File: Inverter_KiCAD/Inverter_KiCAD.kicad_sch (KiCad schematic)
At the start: 0 parts

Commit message: add break
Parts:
- added H1, H2, H3, H4, H5, H6, H7, H8: MountingHole_Pad, symbol Mechanical:MountingHole_Pad
- added J6: Conn_01x03, symbol Connector_Generic:Conn_01x03
- added J7: Conn_01x04, symbol Connector_Generic:Conn_01x04
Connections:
- net GND: now also H5.1, H6.1, H7.1, H8.1, J6.1 (Pin_1)
- net ISO_GND: now also H1.1, H2.1, H3.1, H4.1
- net U_output: now also J7.2 (Pin_2)
- net V_output: now also J7.3 (Pin_3)
- net W_output: now also J7.4 (Pin_4)
- new net Earth: J6.3 (Pin_3), J7.1 (Pin_1)
- new net VSupply_BB: J6.2 (Pin_2)
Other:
- added sheet break (break.kicad_sch)
- added sheet pwrSupplyFiltering (pwrSupplyFiltering.kicad_sch)
- sheet MCU_STM32G474 ports: added Bus_Imes, Bus_V, IC_PWN_U_H, IC_PWN_U_L, IC_PWN_V_H, IC_PWN_V_L, IC_PWN_W_H, IC_PWN_W_L, ISO_3V3, ISO_GND, ISO_PWM_Break, Nucleo_NRST, Nucleo_Rx, Nucleo_Tx, Pwr_Enable, U_Imes, U_VPh, V_Imes, V_VPh, W_Imes, W_VPh; removed none
- sheet Vbus_Sense ports: added ISO_3.3V, Imes, V_Bus_In, V_Bus_Out; removed VBus
- note added: "Break for reverse current protection"
- note added: "Bus mesurement Current and voltage"
- note added: "Chopper 3x Half-bridges"
- note added: "Input Supply and DC/DC converters"
- note added: "Isolated Side"
- note added: "Mounting Holes"
- note added: "NUCLEO for student programming"
- note added: "Power Side"
- note added: "STM32G474RET6 uC for signals analyse and protection Buttons, leds, screen and rotary encoder connectors"

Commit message: update
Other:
- note added: "Ventilateur Radiateur Mesure de température ???"
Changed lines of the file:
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@@
+    (effects (font (size 1.27 1.27)) (justify left bottom))
+  )
+  (text "Ventilateur\nRadiateur\nMesure de température ???" (at 13.97 171.45 0)
     (effects (font (size 1.27 1.27)) (justify left bottom))
   )

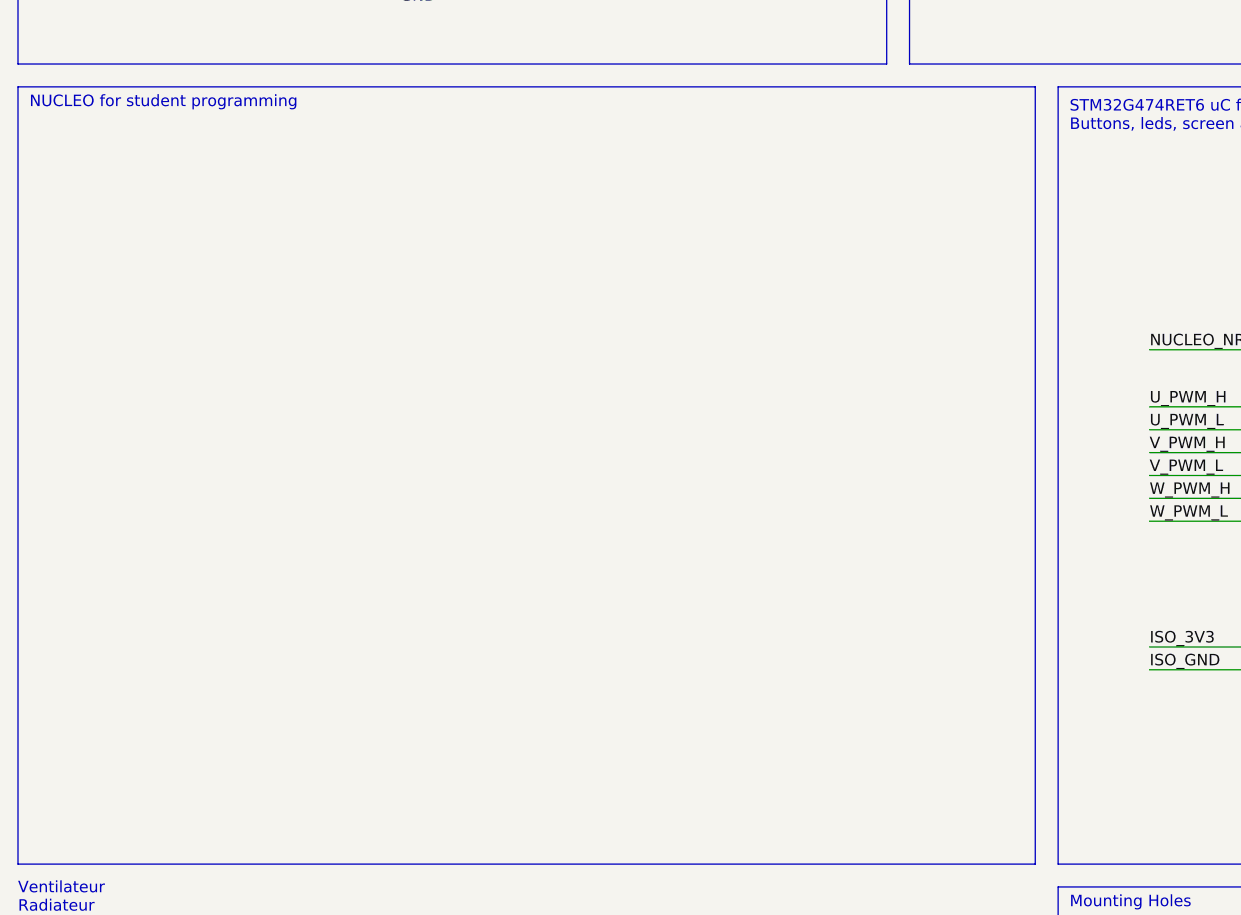
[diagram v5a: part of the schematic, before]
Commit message: start schematic Nucleo board
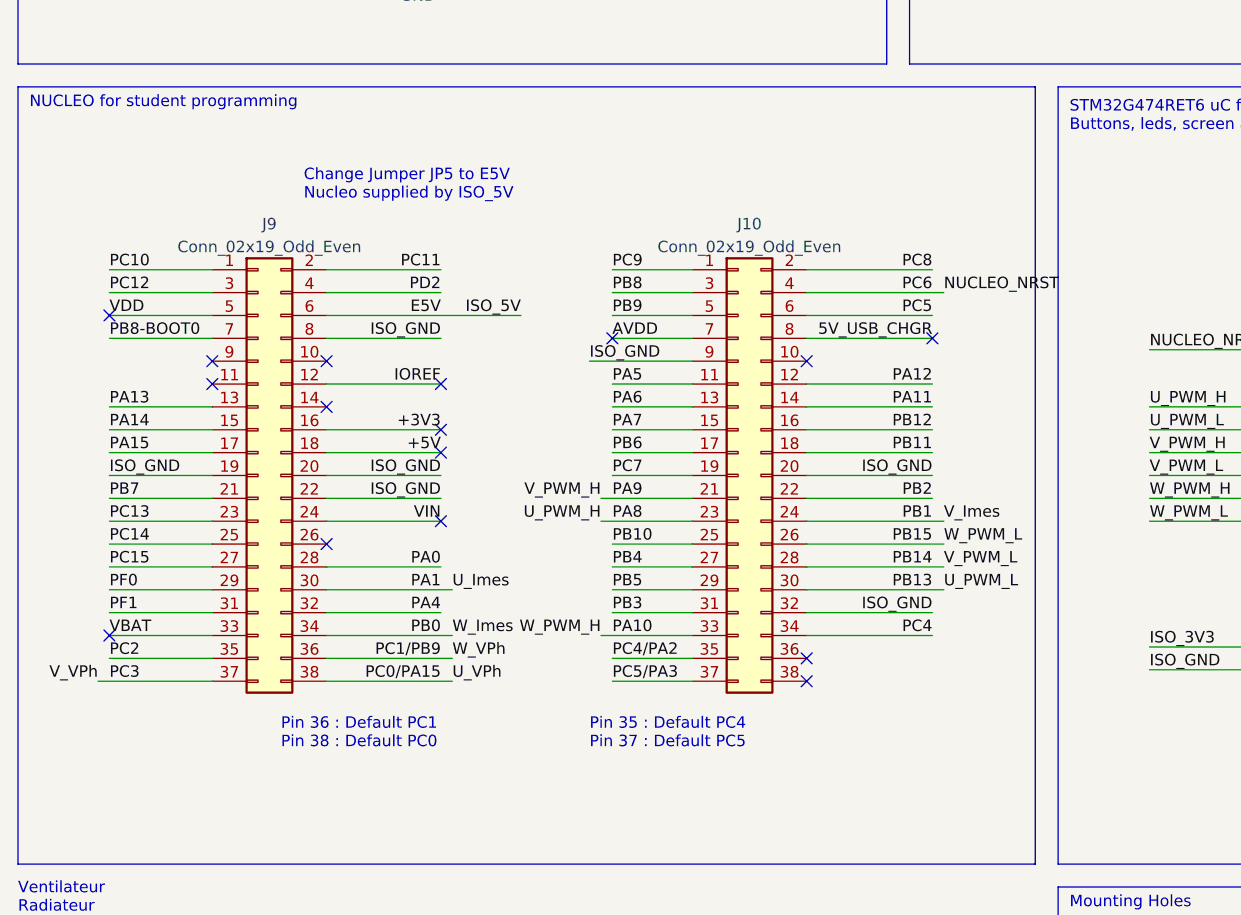
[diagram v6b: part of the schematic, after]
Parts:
- added J10, J9: Conn_02x19_Odd_Even, symbol Connector_Generic:Conn_02x19_Odd_Even
- H1, H2, H3, H4, H5, H6, H7, H8: footprint (none) -> MountingHole:MountingHole_3.2mm_M3_Pad_Via
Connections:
- net ISO_GND: now also J10.20 (Pin_20), J10.32 (Pin_32), J10.9 (Pin_9), J9.19 (Pin_19), J9.20 (Pin_20), J9.22 (Pin_22), J9.8 (Pin_8)
- net NUCLEO_NRST: now also J10.4 (Pin_4)
- new net +3V3: J9.16 (Pin_16)
- new net +5V: J9.18 (Pin_18)
- new net 5V_USB_CHGR: J10.8 (Pin_8)
- new net AVDD: J10.7 (Pin_7)
- new net E5V: J9.6 (Pin_6)
- new net IOREF: J9.12 (Pin_12)
- new net PA0: J9.28 (Pin_28)
- new net PA1: J9.30 (Pin_30)
- new net PA10: J10.33 (Pin_33)
- new net PA11: J10.14 (Pin_14)
- new net PA12: J10.12 (Pin_12)
- new net PA13: J9.13 (Pin_13)
- new net PA14: J9.15 (Pin_15)
- new net PA15: J9.17 (Pin_17)
- new net PA4: J9.32 (Pin_32)
- new net PA5: J10.11 (Pin_11)
- new net PA6: J10.13 (Pin_13)
- new net PA7: J10.15 (Pin_15)
- new net PA8: J10.23 (Pin_23)
- new net PA9: J10.21 (Pin_21)
- new net PB0: J9.34 (Pin_34)
- new net PB1: J10.24 (Pin_24)
- new net PB10: J10.25 (Pin_25)
- new net PB11: J10.18 (Pin_18)
- new net PB12: J10.16 (Pin_16)
- new net PB13: J10.30 (Pin_30)
- new net PB14: J10.28 (Pin_28)
- new net PB15: J10.26 (Pin_26)
- new net PB2: J10.22 (Pin_22)
- new net PB3: J10.31 (Pin_31)
- new net PB4: J10.27 (Pin_27)
- new net PB5: J10.29 (Pin_29)
- new net PB6: J10.17 (Pin_17)
- new net PB7: J9.21 (Pin_21)
- new net PB8: J10.3 (Pin_3)
- new net PB8-BOOT0: J9.7 (Pin_7)
- new net PB9: J10.5 (Pin_5)
- new net PC0/PA15: J9.38 (Pin_38)
- new net PC10: J9.1 (Pin_1)
- new net PC11: J9.2 (Pin_2)
- new net PC12: J9.3 (Pin_3)
- new net PC13: J9.23 (Pin_23)
- new net PC14: J9.25 (Pin_25)
- new net PC15: J9.27 (Pin_27)
- new net PC1/PB9: J9.36 (Pin_36)
- new net PC2: J9.35 (Pin_35)
- new net PC3: J9.37 (Pin_37)
- new net PC4: J10.34 (Pin_34)
- new net PC4/PA2: J10.35 (Pin_35)
- new net PC5: J10.6 (Pin_6)
- new net PC5/PA3: J10.37 (Pin_37)
- new net PC7: J10.19 (Pin_19)
- new net PC8: J10.2 (Pin_2)
- new net PC9: J10.1 (Pin_1)
- new net PD2: J9.4 (Pin_4)
- new net PF0: J9.29 (Pin_29)
- new net PF1: J9.31 (Pin_31)
- new net VBAT: J9.33 (Pin_33)
- new net VDD: J9.5 (Pin_5)
- new net VIN: J9.24 (Pin_24)
- no-connect marks 0 -> 16
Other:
- note added: "Change Jumper JP5 to E5V Nucleo supplied by ISO_5V"
- note added: "Pin 35 : Default PC4 Pin 37 : Default PC5"
- note added: "Pin 36 : Default PC1 Pin 38 : Default PC0"

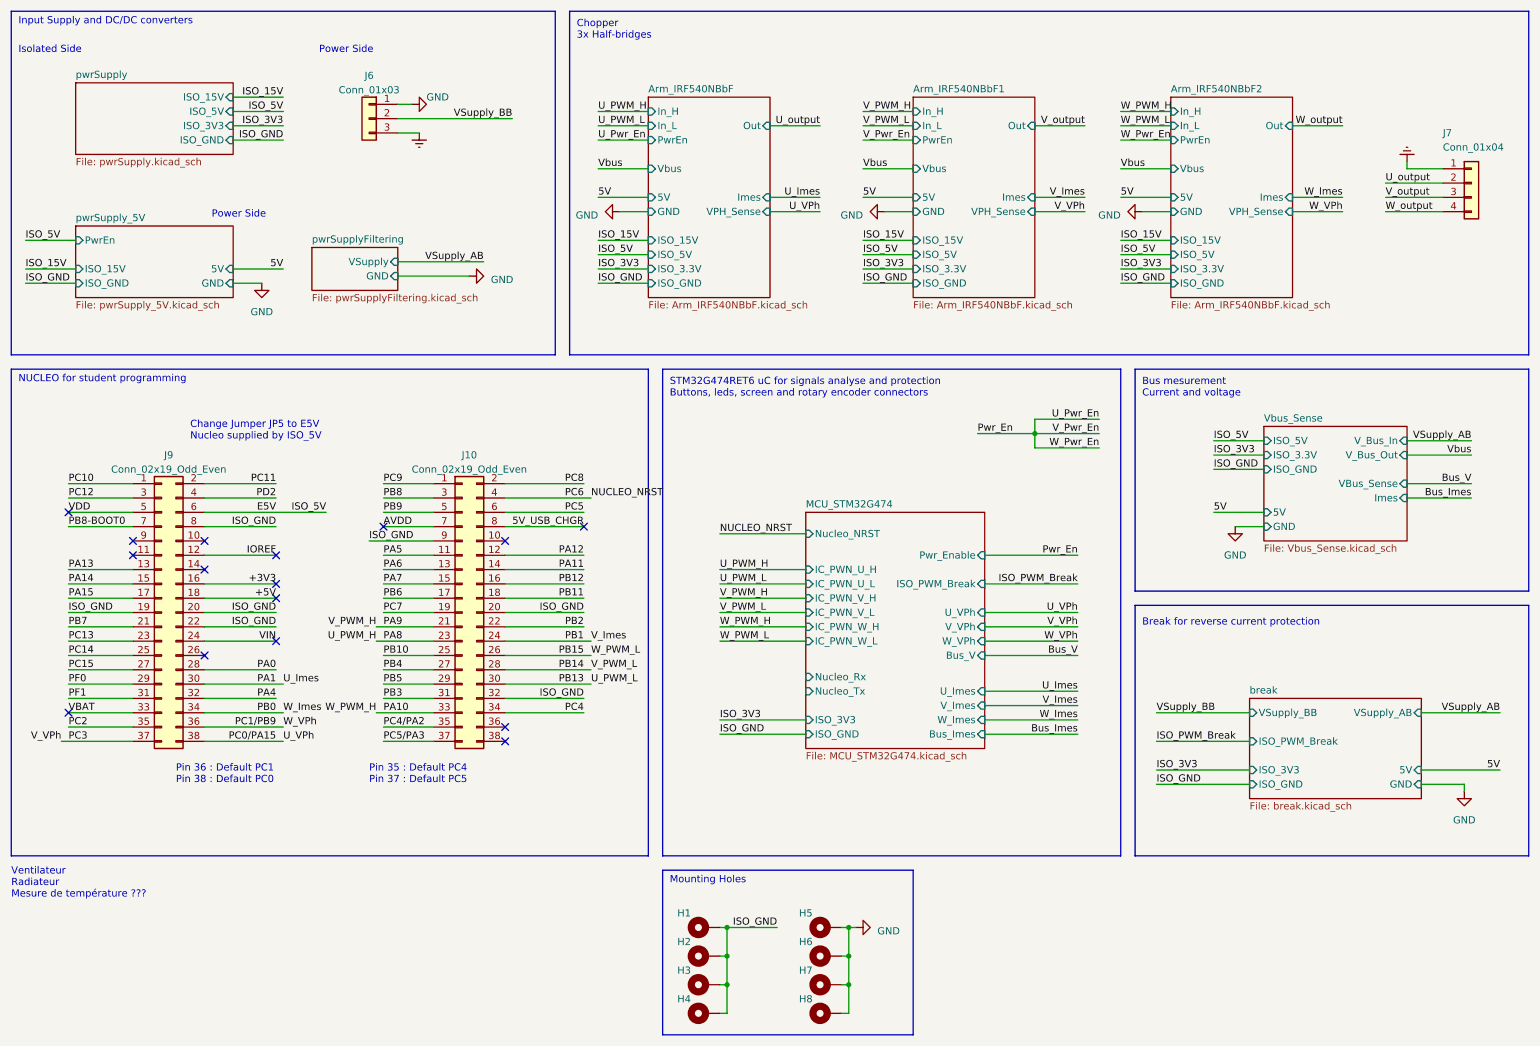
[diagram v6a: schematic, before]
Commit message: clear schematic errors
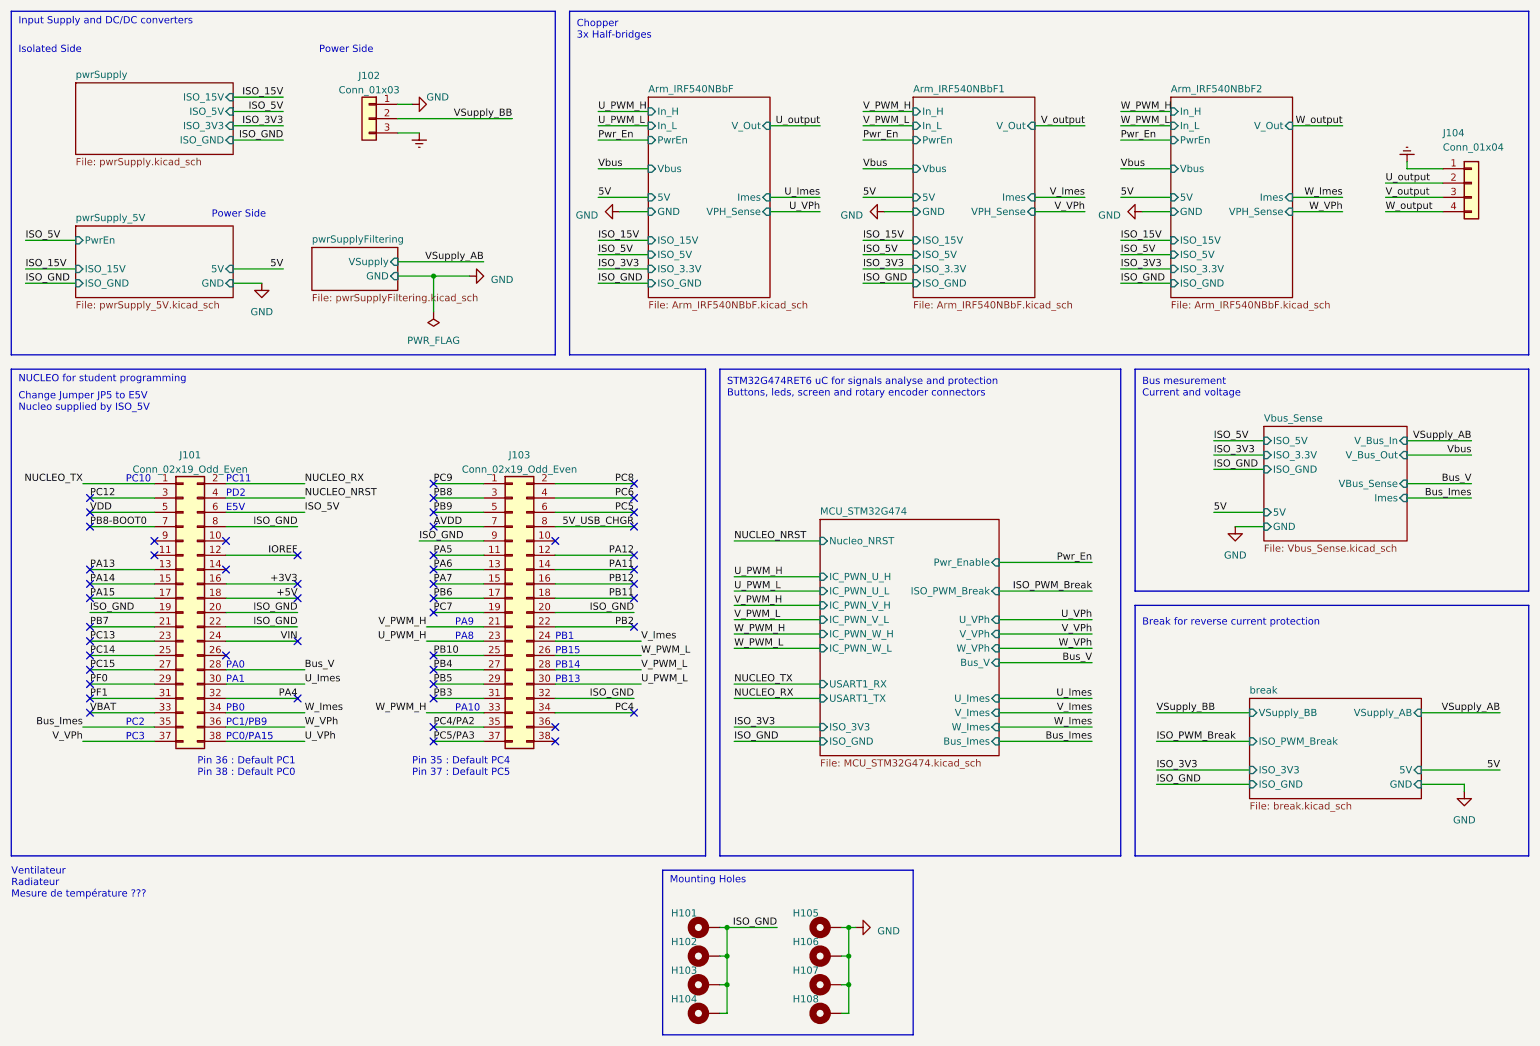
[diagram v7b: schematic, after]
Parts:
- renumbered H1 to H101, H2 to H102, H3 to H103, H4 to H104, H5 to H105, H6 to H106, H7 to H107, H8 to H108, J9 to J101, J6 to J102, J10 to J103, J7 to J104
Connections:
- net PA0 is gone; now on net Bus_V: J101.28 (Pin_28)
- net PC2 is gone; now on net Bus_Imes: J101.35 (Pin_35)
- net PD2 is gone; now on net NUCLEO_NRST: J101.4 (Pin_4)
- net NUCLEO_NRST: no longer J103.4 (Pin_4)
- net E5V renamed ISO_5V
- net PA1 renamed U_Imes
- net PA10 renamed W_PWM_H
- net PA8 renamed U_PWM_H
- net PA9 renamed V_PWM_H
- net PB0 renamed W_Imes
- net PB1 renamed V_Imes
- net PB13 renamed U_PWM_L
- net PB14 renamed V_PWM_L
- net PB15 renamed W_PWM_L
- net PC0/PA15 renamed U_VPh
- net PC10 renamed NUCLEO_TX
- net PC11 renamed NUCLEO_RX
- net PC1/PB9 renamed W_VPh
- net PC3 renamed V_VPh
- new net PC6: J103.4 (Pin_4)
- no-connect marks 16 -> 51
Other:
- sheet Arm_IRF540NBbF ports: added V_Out; removed Out
- sheet Arm_IRF540NBbF1 ports: added V_Out; removed Out
- sheet Arm_IRF540NBbF2 ports: added V_Out; removed Out
- sheet MCU_STM32G474 ports: added USART1_RX, USART1_TX; removed Nucleo_Rx, Nucleo_Tx
- note added: "E5V"
- note added: "PA0"
- note added: "PA1"
- note added: "PA10"
- note added: "PA8"
- note added: "PA9"
- note added: "PB0"
- note added: "PB1"
- note added: "PB13"
- note added: "PB14"
- note added: "PB15"
- note added: "PC0/PA15"
- note added: "PC1/PB9"
- note added: "PC10"
- note added: "PC11"
- note added: "PC2"
- note added: "PC3"
- note added: "PD2"
- moved on the sheet: J101, J103

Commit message: end of sch, start pcb
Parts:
- J101, J103: footprint (none) -> Connector_PinHeader_2.54mm:PinHeader_2x19_P2.54mm_Vertical
- J102: MFR (none) -> 691311700003
- J104: MFR (none) -> 691311700004
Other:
- added sheet FAN (FAN.kicad_sch)
- added sheet tempSensor (tempSensor.kicad_sch)
- sheet MCU_STM32G474 ports: added I2C_SCL, I2C_SDA, ISO_PWM_Fan; removed none
- note added: "FAN 2 outputs"
- note added: "Temperature Sensor based on TCN75A"
- note removed: "Ventilateur Radiateur Mesure de température ???"
- company: (none) -> ENSEA
- title: (none) -> AAP Inverter
